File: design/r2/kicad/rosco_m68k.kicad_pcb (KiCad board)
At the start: 4 copper layers, 160 x 100 mm, 93 parts, among them IC1 MC68010P10, IC15 555N, IC2 ATF22V10C, IC3 ATF22V10C, IC4 XR68C681CJTR-F, IC5 ATF22V10C, IC6 ATF22V10C, IC7 74LS148, J1 UART_A, J2 UART_B, J3 Conn_02x32_Odd_Even, J4 Conn_01x06, J5 PWR, J6 Conn_01x04_Male, J7 Conn_01x01_Male, Q1 Crystal, Q2 5H8ET-10.000, U1 SST39SF040, U2 SST39SF040, U3 AS6C4008-55PCN, U4 AS6C4008-55PCN

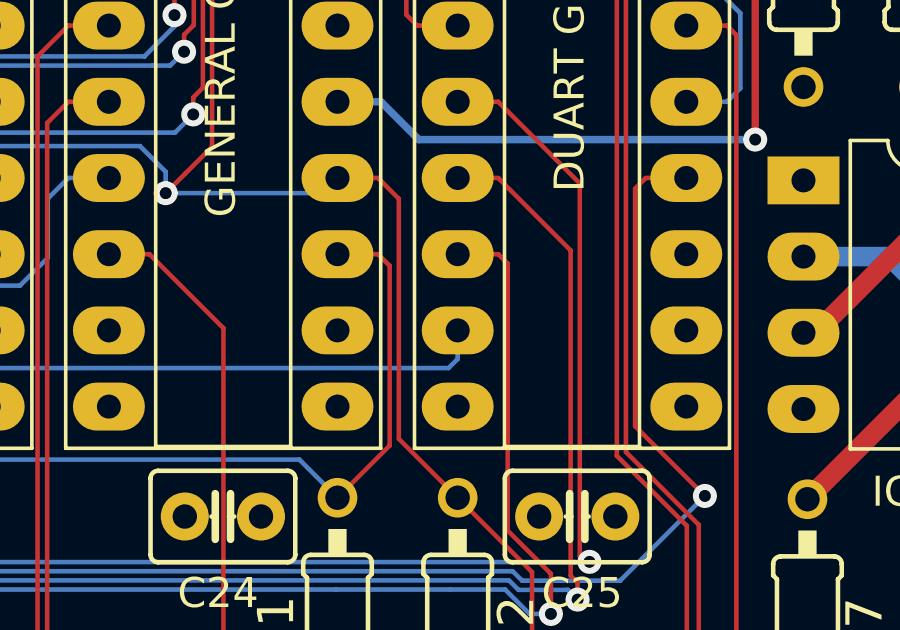
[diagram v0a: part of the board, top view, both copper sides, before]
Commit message: Fully decode for DUART
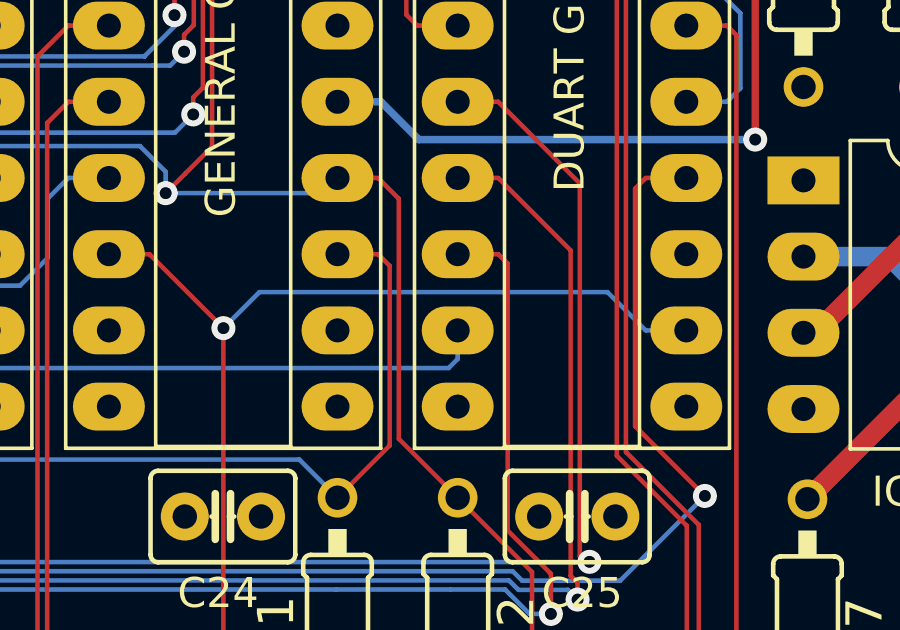
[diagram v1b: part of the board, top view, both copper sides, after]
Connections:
- IC3 pad 14: Net-(IC3-Pad14) -> A19
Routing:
- net A19: track 304.2 -> 320.6 mm, vias 5 -> 6

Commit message: Fix unconnected VCC on 148
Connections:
- IC7 pad 16: Net-(IC7-Pad16) -> VCC
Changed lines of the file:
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@@
     (zones 0)
     (modules 93)
-    (nets 152)
+    (nets 151)
   )
   (page A4)
@@
   )
   (setup
-    (last_trace_width 0.1524)
+    (last_trace_width 0.25)
     (user_trace_width 0.1524)
     (user_trace_width 0.65)
@@
   (net 149 IRQ6)
   (net 150 IRQ5)
-  (net 151 "Net-(IC7-Pad16)")
   (net_class Default "This is the default net class."
     (clearance 0.1524)
@@
     (add_net "Net-(IC7-Pad14)")
     (add_net "Net-(IC7-Pad15)")
-    (add_net "Net-(IC7-Pad16)")
     (add_net "Net-(LED1-PadA)")
     (add_net "Net-(LED2-PadA)")
@@
     (fp_arc (start 3.81 -1.33) (end 2.81 -1.33) (angle -180) (layer F.SilkS) (width 0.12))
     (pad 16 thru_hole oval (at 7.62 0 90) (size 2.4 1.6) (drill 0.8) (layers *.Cu *.Mask)
-      (net 151 "Net-(IC7-Pad16)"))
+      (net 17 VCC))
     (pad 8 thru_hole oval (at 0 17.78 90) (size 2.4 1.6) (drill 0.8) (layers *.Cu *.Mask)
       (net 18 GND))

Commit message: Super-minor tidy-up
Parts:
- C1, C2: footprint rosco_m68k:C2.5-3 -> rosco_m68k:C2.5_or_3.5-3
- H1, H2, H3, H4: footprint MountingHole:MountingHole_3.2mm_M3 -> MountingHole:MountingHole_3.2mm_M3_Pad
- Q1: value Crystal -> 3.6864MHz
- moved C32 11.7 mm to (199.1, 146.1)
- moved C2 8.49 mm to (202.2, 138.4)
- moved Q1 5.45 mm to (190.8, 138.4)
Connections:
- C2 pad 1: Net-(C2-Pad1) -> GND
- C2 pad 2: GND -> Net-(C2-Pad2)
- H1 pad 1: (no net) -> GND
- H2 pad 1: (no net) -> GND
- H3 pad 1: (no net) -> GND
- H4 pad 1: (no net) -> GND
- IC4 pad 37: Net-(C2-Pad1) -> Net-(C2-Pad2)
- Q1 pad 2: Net-(C2-Pad1) -> Net-(C2-Pad2)
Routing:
- net Net-(C2-Pad1): track 20.5 -> 0.00 mm
- net Net-(C2-Pad2): track 0.00 -> 16.5 mm
- net GND: track 94.0 -> 103.1 mm
- net Net-(C1-Pad2): track 24.7 -> 20.1 mm
- net Net-(IC4-Pad15): track 70.8 -> 72.9 mm
- net Net-(IC4-Pad16): track 52.9 -> 54.9 mm
- net IOSEL: track 192.7 -> 192.0 mm
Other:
- board text added: "Copyright ©2019-2022"
- board text added: "Revision 2.12 (January 2022)"
- board text added: "revision 2.12"
- board text removed: "Copyright ©2021"
- board text removed: "Revision 2.1 (November 2021)"
- board text removed: "revision 2.0"
